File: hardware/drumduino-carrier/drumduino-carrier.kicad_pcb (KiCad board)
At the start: 2 copper layers, 100 x 100 mm, 53 parts, among them J1 IN A0 CRASH, J10 IN A9 RIDE BELL, J11 IN A10 AUX, J12 IN A11 AUX, J13 IN A12 AUX, J14 IN A13 AUX, J15 IN A14 AUX, J16 HH PEDAL (wiper/VCC/GND), J2 IN A1 HIHAT, J3 IN A2 SNARE, J4 IN A3 KICK, J5 IN A4 TOM1, J6 IN A5 TOM2, J7 IN A6 FLOOR, J8 IN A7 RIDE, J9 IN A8 SN RIM, U1 MEGA2560_PRO

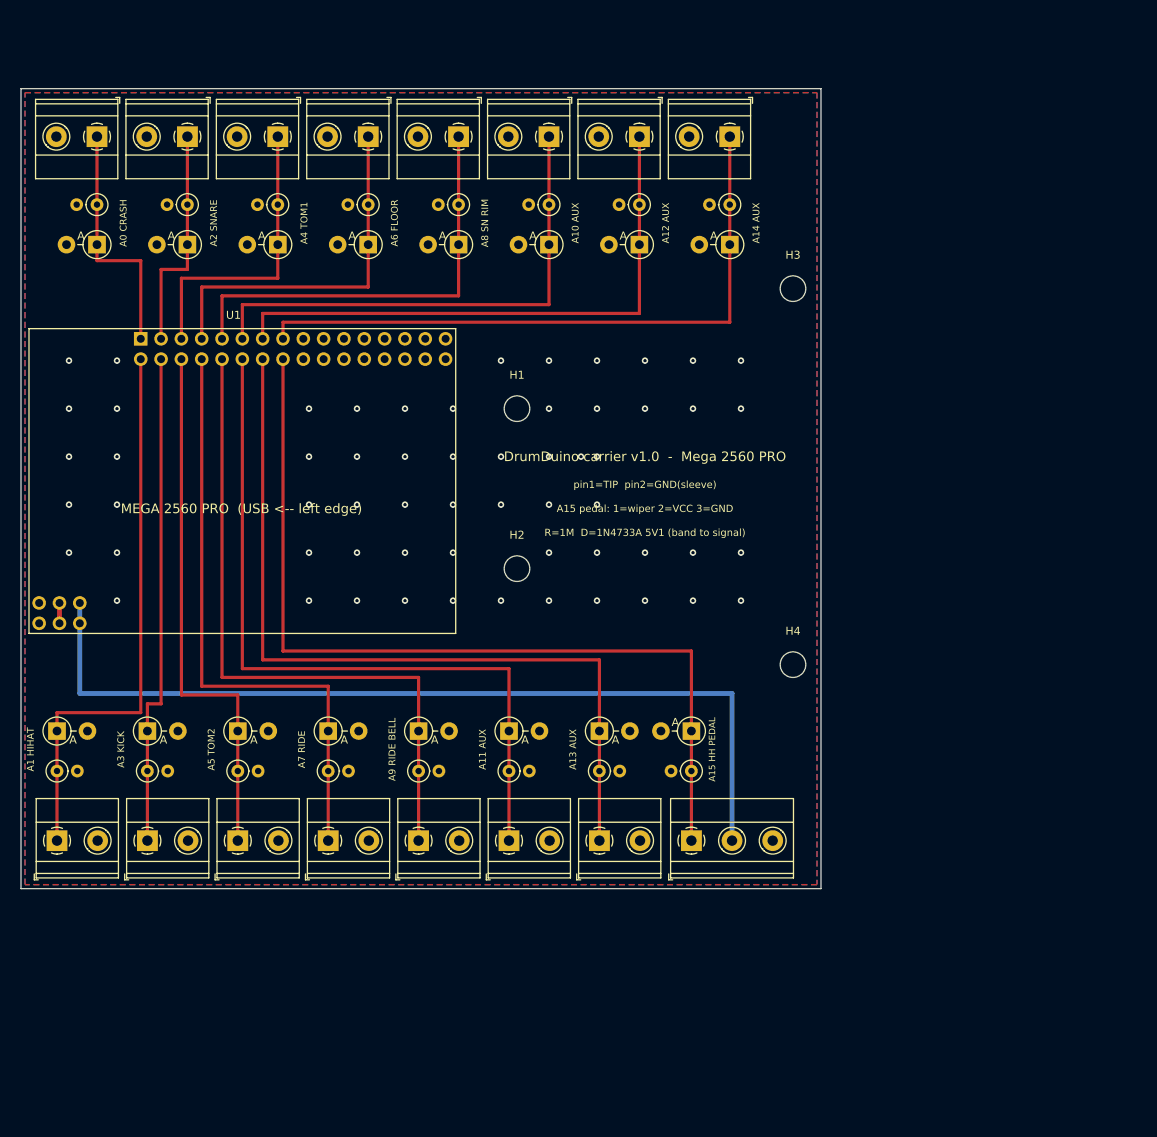
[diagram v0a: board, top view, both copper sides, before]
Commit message: Carrier v2: 16 Rean NRJ6HF edge jacks, DC 9V input with 1N5819, local 3D models (incl. Mega 2560 PRO)
Co-Authored-By: Claude Opus 5.5 <noreply@anthropic.com>
Claude-Session: https://claude.ai/code/session_019Dkdmctnzo4hmTgGEA8k6P
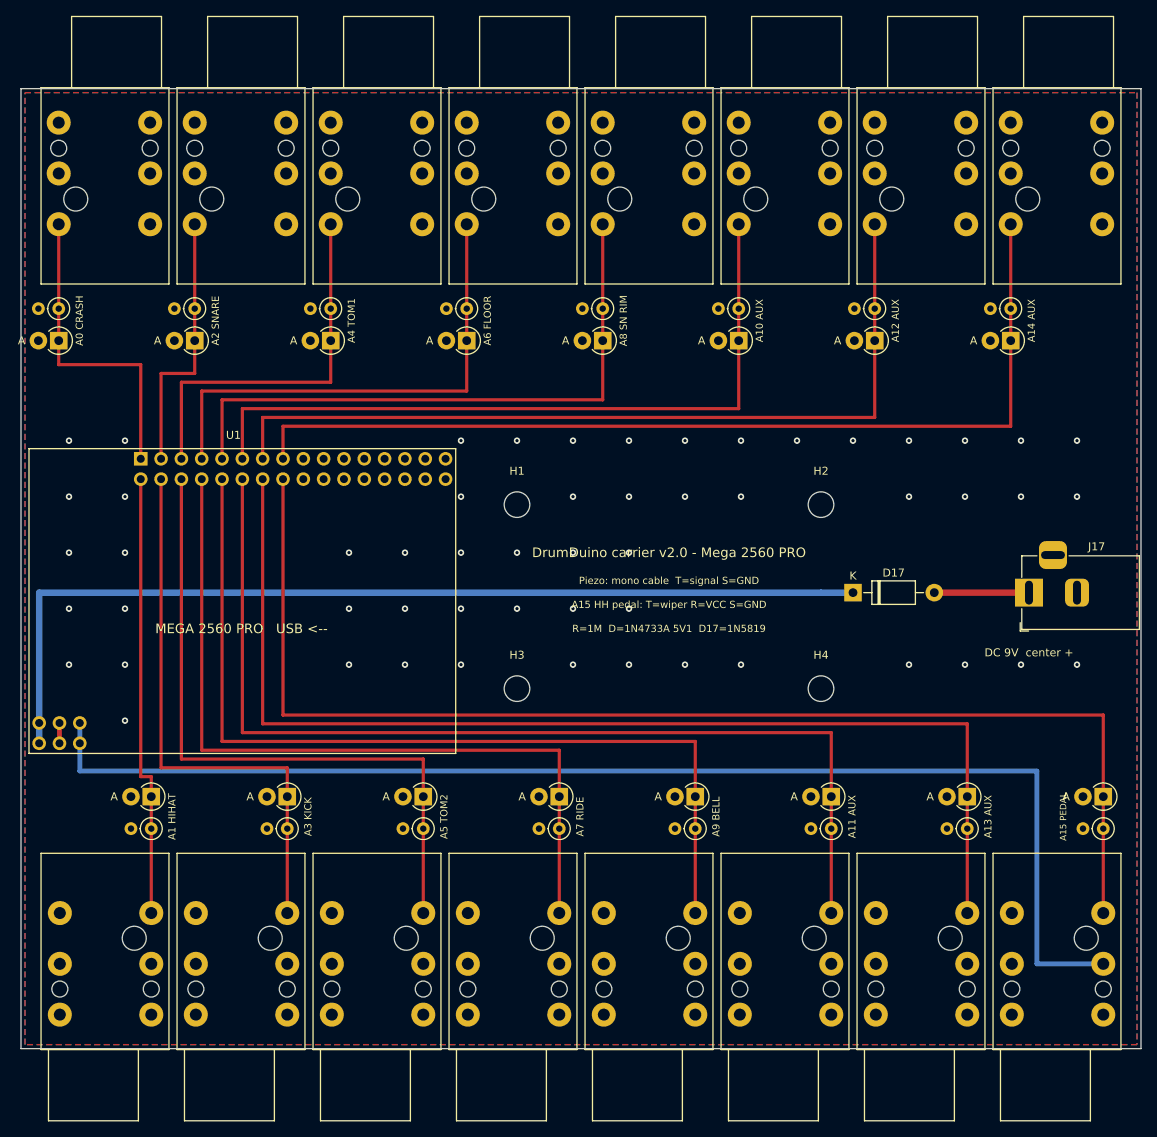
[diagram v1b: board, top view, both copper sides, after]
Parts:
- added D17: 1N5819, Diode_THT:D_DO-41_SOD81_P10.16mm_Horizontal, F.Cu at (104.0, 63.0)
- added J17: DC 5.5x2.1 9V, Connector_BarrelJack:BarrelJack_Horizontal, F.Cu at (126.0, 63.0)
- D1, D10, D11, D12, D13, D14, D15, D16, D2, D3, D4, D5, D6, D7, D8, D9: footprint Diode_THT:D_DO-41_SOD81_P3.81mm_Vertical_AnodeUp -> Diode_THT:D_DO-41_SOD81_P2.54mm_Vertical_AnodeUp
- J1, J11, J12, J13, J14, J15, J2, J3, J4, J5, J6, J7, J8, J9: footprint TerminalBlock_Phoenix:TerminalBlock_Phoenix_MKDS-1,5-2-5.08_1x02_P5.08mm_Horizontal -> Connector_Audio:Jack_6.35mm_Neutrik_NRJ6HF_Horizontal
- J10: value IN A9 RIDE BELL -> IN A9 BELL; footprint TerminalBlock_Phoenix:TerminalBlock_Phoenix_MKDS-1,5-2-5.08_1x02_P5.08mm_Horizontal -> Connector_Audio:Jack_6.35mm_Neutrik_NRJ6HF_Horizontal
- J16: value HH PEDAL (wiper/VCC/GND) -> HH PEDAL (T=wiper R=VCC S=GND); footprint TerminalBlock_Phoenix:TerminalBlock_Phoenix_MKDS-1,5-3-5.08_1x03_P5.08mm_Horizontal -> Connector_Audio:Jack_6.35mm_Neutrik_NRJ6HF_Horizontal
- moved H3 60.7 mm to (62.0, 75.0)
- moved J16 52.3 mm to (135.3, 103.0), turned to -90 degrees
- moved D16 52.1 mm to (135.3, 88.5)
- moved R16 52.0 mm to (135.3, 92.5)
- moved J14 46.9 mm to (118.3, 103.0), turned to -90 degrees
- moved D14 46.7 mm to (118.3, 88.5), turned to 180 degrees
- moved R14 46.5 mm to (118.3, 92.5), turned to 180 degrees
- moved J12 41.3 mm to (101.3, 103.0), turned to -90 degrees
- moved D12 41.1 mm to (101.3, 88.5), turned to 180 degrees
- moved R12 40.9 mm to (101.3, 92.5), turned to 180 degrees
- moved H2 38.8 mm to (100.0, 52.0)
- moved R15 37.4 mm to (123.7, 27.5)
- moved D15 37.1 mm to (123.7, 31.5)
- moved J15 36.8 mm to (123.7, 16.9), turned to 90 degrees
- moved J10 35.7 mm to (84.3, 103.0), turned to -90 degrees
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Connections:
- U1 pad VIN: (no net) -> VIN
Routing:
- net VIN: track 0.00 -> 120.6 mm
- net VCC: track 111.2 -> 158.0 mm
- net A15: track 111.2 -> 156.8 mm
- net A13: track 102.3 -> 142.3 mm
- net A14: track 81.1 -> 120.3 mm
- net A11: track 93.5 -> 127.9 mm
- net A12: track 72.4 -> 105.8 mm
- net A9: track 84.8 -> 113.4 mm
- net A10: track 63.6 -> 91.4 mm
- net A7: track 76.0 -> 98.9 mm
- net A8: track 54.8 -> 76.9 mm
- net A5: track 67.2 -> 84.5 mm
- net A6: track 46.1 -> 62.4 mm
- net A1: track 70.7 -> 55.6 mm
- net VRAW: track 0.00 -> 11.8 mm
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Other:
- board size 100 x 100 mm -> 140 x 120 mm
- board text added: "A15 HH pedal: T=wiper R=VCC S=GND"
- board text added: "A15 PEDAL"
- board text added: "A9 BELL"
- board text added: "DC 9V center +"
- board text added: "DrumDuino carrier v2.0 - Mega 2560 PRO"
- board text added: "Piezo: mono cable T=signal S=GND"
- board text added: "R=1M D=1N4733A 5V1 D17=1N5819"
- board text removed: "A15 HH PEDAL"
- board text removed: "A15 pedal: 1=wiper 2=VCC 3=GND"
- board text removed: "A9 RIDE BELL"
- board text removed: "DrumDuino carrier v1.0 - Mega 2560 PRO"
- board text removed: "R=1M D=1N4733A 5V1 (band to signal)"
- board text removed: "pin1=TIP pin2=GND(sleeve)"
